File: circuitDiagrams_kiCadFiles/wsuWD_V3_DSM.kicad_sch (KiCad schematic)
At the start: 46 parts, among them J1 USB_A, J2 Screw Terminal, U1 LD1086D2M33TR, U2 LD1086DT50TR, U3 TCAN332, U4 FT232RL, U5 ATmega644PA-AU, U6 ASDMB-16.000MHz-LC-T, U7 MAX7219, U8 MCP2515-xSO

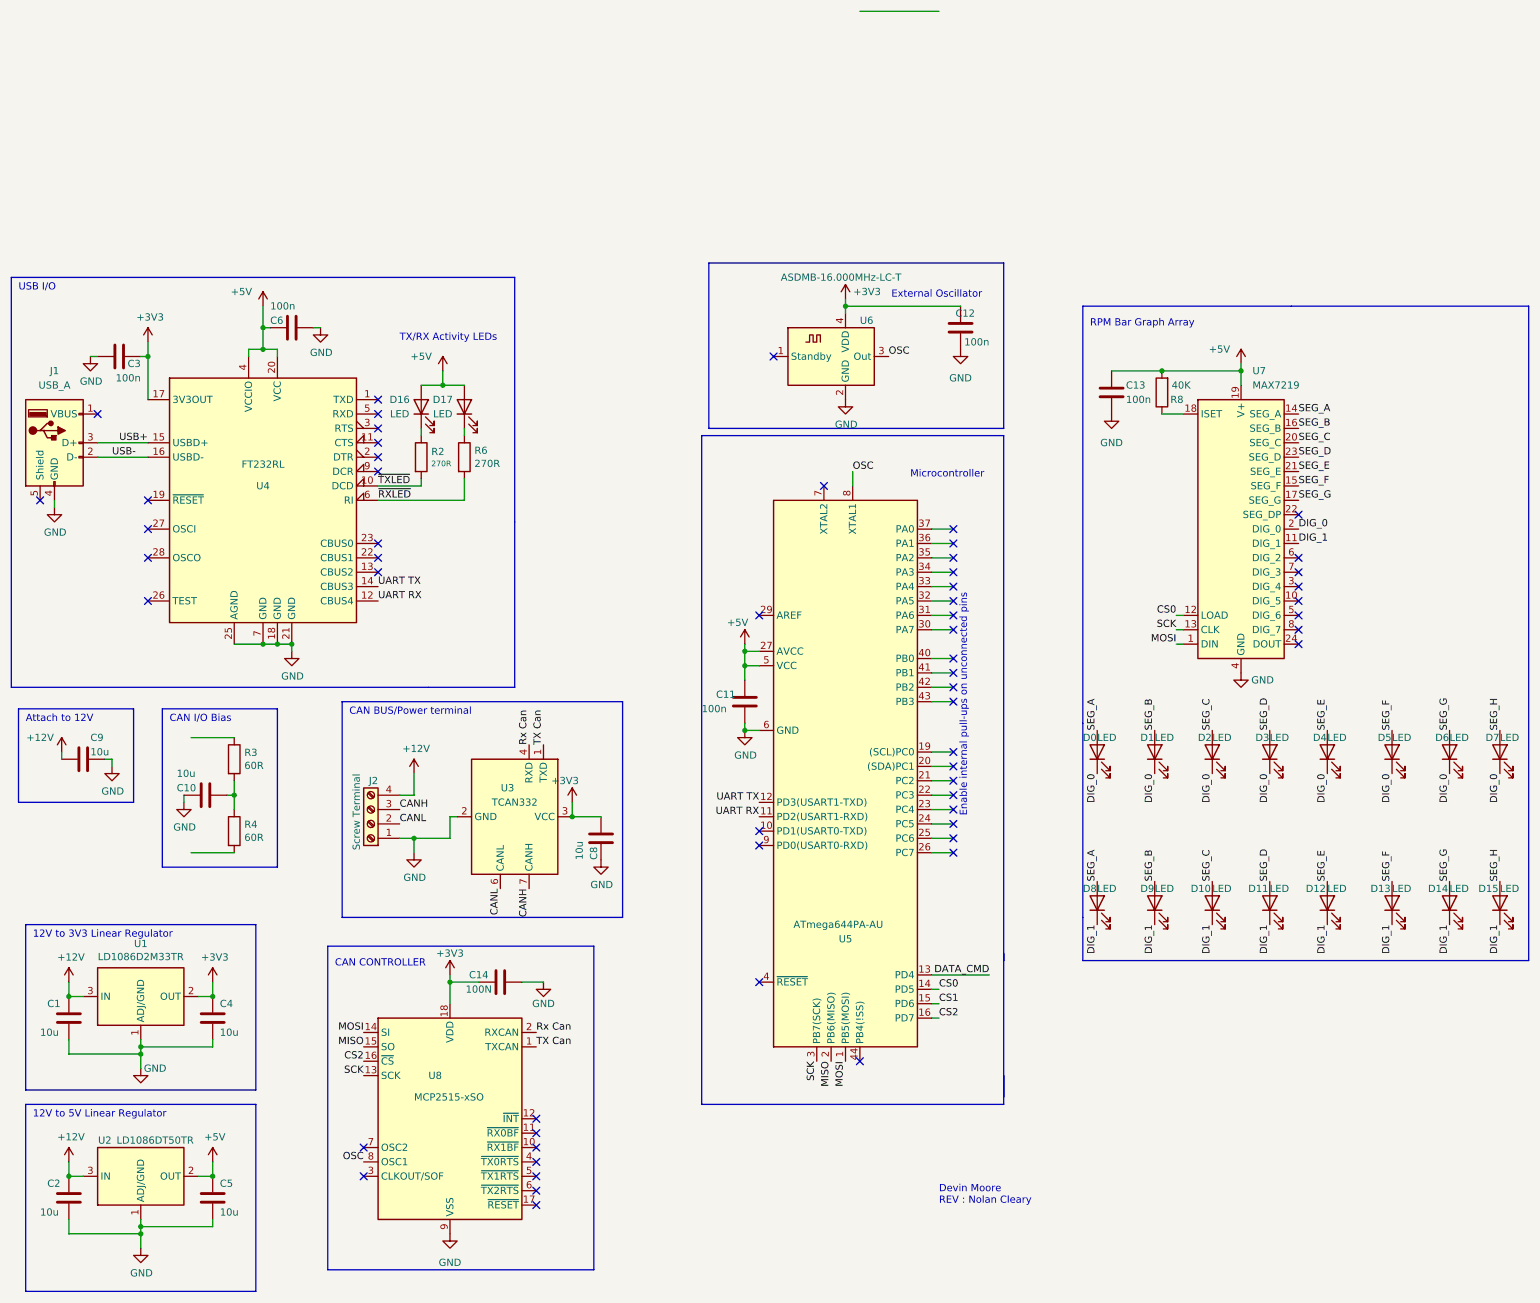
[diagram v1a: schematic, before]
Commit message: Update wsuWD_V3_DSM.kicad_sch
Changed Components and added all footprints
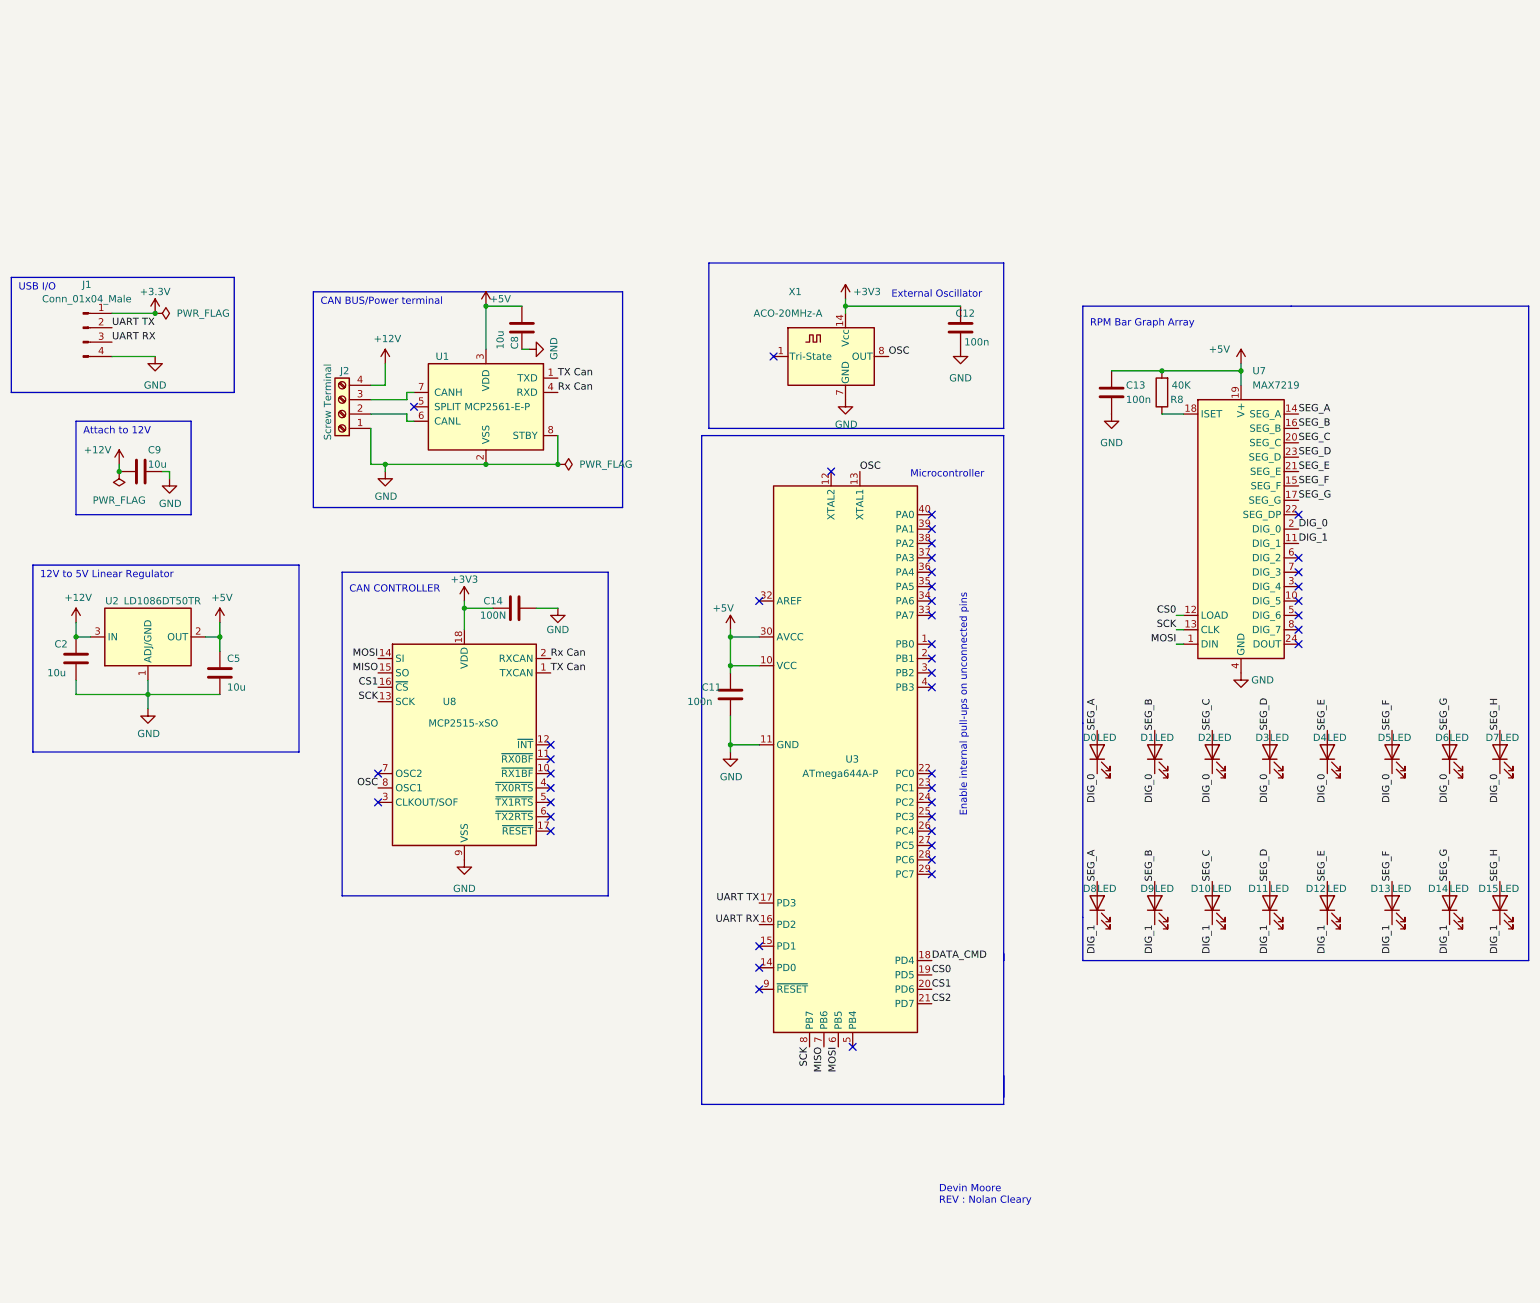
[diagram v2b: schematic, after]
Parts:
- removed C1, C10, C4: 10u, symbol Device:C
- removed C3, C6: 100n, symbol Device:C
- removed D16, D17: LED, symbol Device:LED
- removed J1: USB_A, symbol Connector:USB_A
- removed R2, R6: 270R, symbol Device:R
- removed R3, R4: 60R, symbol Device:R
- removed U1: LD1086D2M33TR, Package_TO_SOT_SMD:TO-263-3_TabPin2, symbol Regulator_Linear:LD1086D2M33TR
- removed U3: TCAN332, symbol Interface_CAN_LIN:TCAN332
- removed U4: FT232RL, Package_SO:SSOP-28_5.3x10.2mm_P0.65mm, symbol Interface_USB:FT232RL
- removed U5: ATmega644PA-AU, Package_QFP:TQFP-44_10x10mm_P0.8mm, symbol MCU_Microchip_ATmega:ATmega644PA-AU
- removed U6: ASDMB-16.000MHz-LC-T, Oscillator:Oscillator_SMD_Abracon_ASDMB-4Pin_2.5x2.0mm, symbol Oscillator:ASDMB-xxxMHz
- added J1: Conn_01x04_Male, Connector_PinHeader_2.54mm:PinHeader_1x04_P2.54mm_Vertical, symbol Connector:Conn_01x04_Male
- added U1: MCP2561-E-P, Package_DIP:DIP-8_W7.62mm, symbol Interface_CAN_LIN:MCP2561-E-P
- added U3: ATmega644A-P, Package_DIP:DIP-40_W15.24mm, symbol MCU_Microchip_ATmega:ATmega644A-P
- added X1: ACO-20MHz-A, Oscillator:Oscillator_DIP-14, symbol Oscillator:ACO-xxxMHz-A
- J2: footprint (none) -> TerminalBlock_4Ucon:TerminalBlock_4Ucon_1x04_P3.50mm_Horizontal
- U7: footprint (none) -> Package_DIP:DIP-24_W7.62mm
- U8: footprint Package_SO:SOIC-18W_7.5x11.6mm_P1.27mm -> Package_DIP:DIP-18_W7.62mm
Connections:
- net +3V3: now also J1.1 (Pin_1), X1.14 (Vcc); no longer C8.1
- net +5V: now also C8.1, U1.3 (VDD), U3.10 (VCC), U3.30 (AVCC)
- net CS0: now also U3.19 (PD5)
- net CS1: now also U8.16 (~{CS}), U3.20 (PD6)
- net CS2: now also U3.21 (PD7); no longer U8.16 (~{CS})
- net DATA_CMD: now also U3.18 (PD4)
- net GND: now also J1.4 (Pin_4), U1.2 (VSS), U1.8 (STBY), U3.11 (GND), X1.7 (GND)
- net MISO: now also U3.7 (PB6)
- net MOSI: now also U3.6 (PB5)
- net OSC: now also U3.13 (XTAL1), X1.8 (OUT)
- net Rx Can: now also U1.4 (RXD)
- net SCK: now also U3.8 (PB7)
- net TX Can: now also U1.1 (TXD)
- net UART RX: now also J1.3 (Pin_3), U3.16 (PD2)
- net UART TX: now also J1.2 (Pin_2), U3.17 (PD3)
- net CANH: no longer names the net of J2.3 (Pin_3)
- net CANH: now also U1.7 (CANH)
- net CANL: no longer names the net of J2.2 (Pin_2)
- net CANL: now also U1.6 (CANL)
- no-connect marks 59 -> 45
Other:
- note removed: "12V to 3V3 Linear Regulator"
- note removed: "CAN I/O Bias"
- note removed: "TX/RX Activity LEDs"
- moved on the sheet: C11, C14, C2, C5, C8, C9, J2, U2, U8
